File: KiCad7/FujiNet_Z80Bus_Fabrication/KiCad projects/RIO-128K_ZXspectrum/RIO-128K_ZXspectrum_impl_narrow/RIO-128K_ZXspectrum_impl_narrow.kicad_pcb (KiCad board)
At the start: 2 copper layers, 45 x 95 mm, 8 parts, among them J1 Conn_01x24_Socket, J2 Conn_01x18_Socket

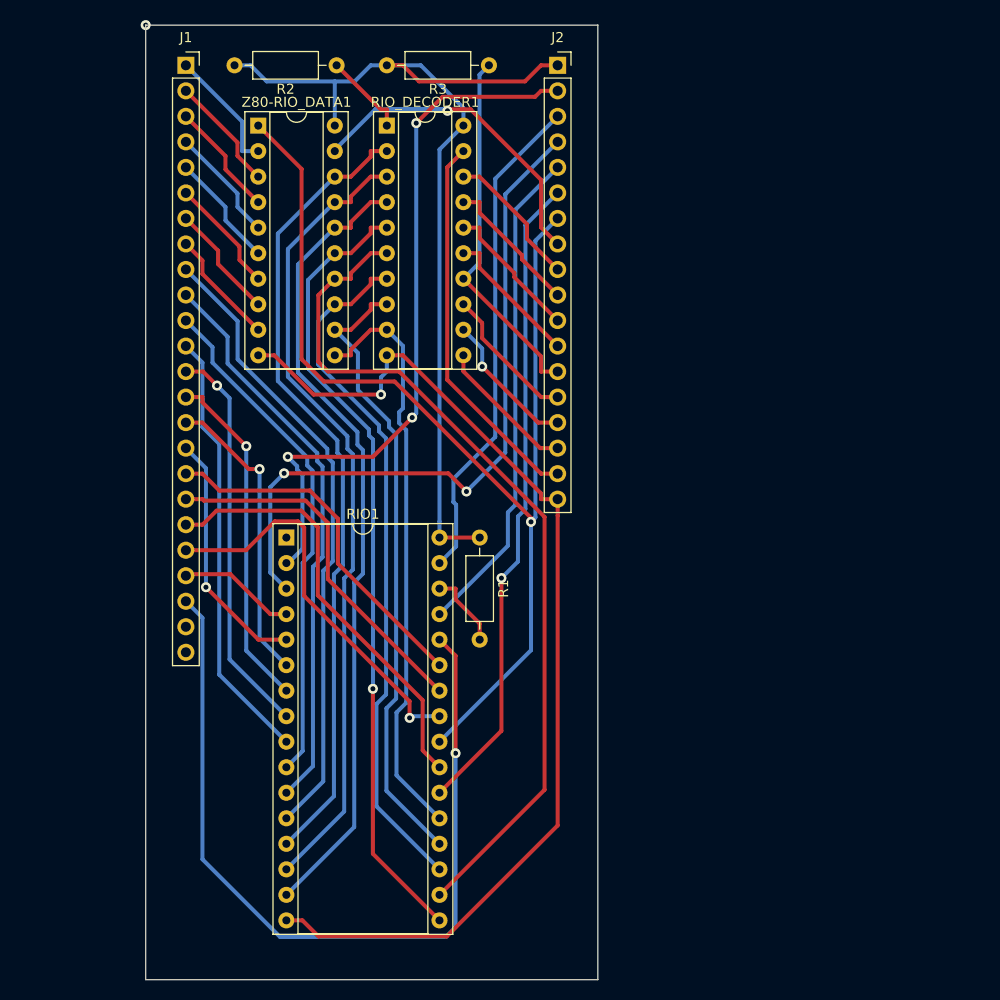
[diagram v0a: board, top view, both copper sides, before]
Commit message: KiCad Corrected the orientation of the impl PCBs
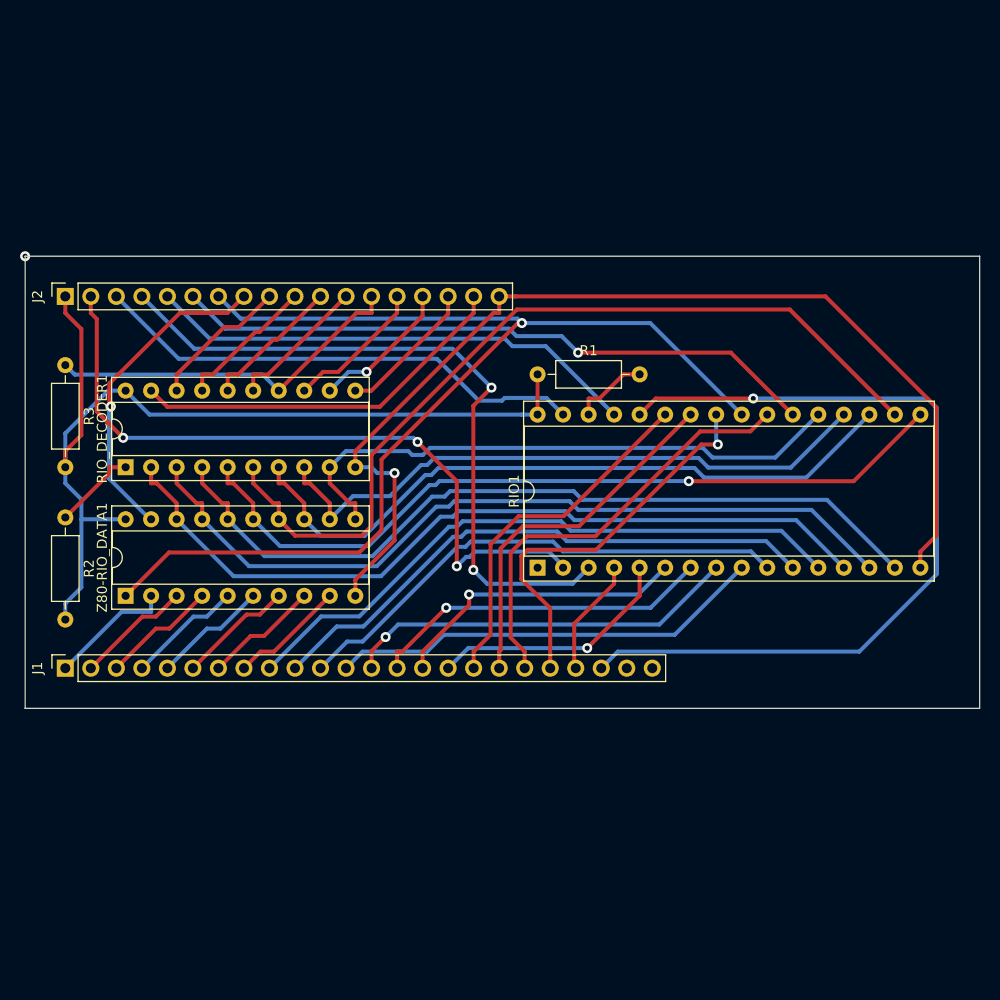
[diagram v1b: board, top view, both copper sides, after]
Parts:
- moved J1 61.2 mm to (103.0, 130.0), turned to 90 degrees
- moved J2 54.1 mm to (103.0, 93.0), turned to 90 degrees
- moved R2 52.5 mm to (103.0, 115.0), turned to -90 degrees
- moved R3 51.7 mm to (103.0, 99.8), turned to -90 degrees
- moved Z80-RIO_DATA1 48.6 mm to (109.0, 122.8), turned to 90 degrees
- moved RIO_DECODER1 42.8 mm to (109.0, 110.0), turned to 90 degrees
- moved RIO1 25.2 mm to (150.0, 120.0), turned to 90 degrees
- moved R1 17.2 mm to (150.0, 100.8), turned to 0 degrees
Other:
- board size 45 x 95 mm -> 95 x 45 mm
